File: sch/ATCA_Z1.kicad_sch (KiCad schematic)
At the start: 1 part, among them P10 1766500-1

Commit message: added magjacks
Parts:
- P10: footprint KIT_Connector:TE_1766500-1 -> project:TE_1766500-1
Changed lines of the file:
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@@
       (effects (font (size 1.27 1.27)))
     )
-    (property "Footprint" "KIT_Connector:TE_1766500-1" (at 144.78 92.71 0)
+    (property "Footprint" "project:TE_1766500-1" (at 144.78 92.71 0)
       (effects (font (size 1.27 1.27)) hide)
     )

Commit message: Project recovered
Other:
- title: ATCA Template -> ATCA Simple Loopback HUB
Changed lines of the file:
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@@
   (paper "A4")
   (title_block
-    (title "ATCA Template")
-    (date "2023-07-20")
+    (title "ATCA Simple Loopback HUB")
+    (date "2023-09-12")
     (rev "1.0")
     (company "Karlsruhe Institute of Technology (KIT)")
     (comment 1 "Institute for Data Processing and Electronics (IPE)")
     (comment 2 "Luis Ardila")
-    (comment 4 "Licensed under CERN-OHL-S-2.0")
+    (comment 3 "IPE-380-06")
+    (comment 4 "Licensed under CERN-OHL-P-2.0")
   )
   (no_connect (at 127 120.65))
@@
     (pin "9")
     (instances
-      (project "atca_simple_hub"
+      (project "atca-simple-loopback-hub"
         (path "/b1bf14e0-f6d2-45a7-b67f-6500a354b7ad/248439bf-2e2f-4e24-b510-c03a1ea34b90"
           (reference "P10") (unit 1)

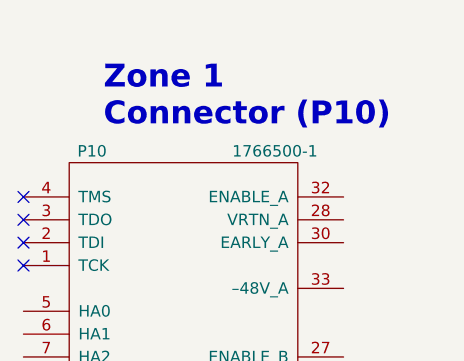
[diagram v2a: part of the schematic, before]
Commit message: organization of sub sheets
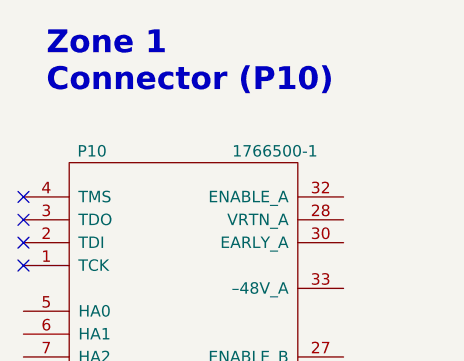
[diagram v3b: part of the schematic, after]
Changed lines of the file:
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@@
   (no_connect (at 127 107.95))
   (no_connect (at 127 110.49))
-  (text "Zone 1 \nConnector (P10)" (at 135.89 59.69 0)
+  (text "Zone 1 \nConnector (P10)" (at 129.54 55.88 0)
     (effects (font (size 2.54 2.54) (thickness 0.508) bold) (justify left bottom))
   )

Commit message: sch work
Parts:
- added C57, C58, C59, C60: 2.2uF, Capacitor_SMD:C_1206_3216Metric, symbol Device:C
- added C61, C62, C77, C78: 20nF, Capacitor_SMD:C_0805_2012Metric, symbol Device:C
- added C79, C80, C81: 100uF, Capacitor_THT:CP_Radial_D16.0mm_P7.50mm, symbol Device:C_Polarized
- added C82, C84: 22uF, Capacitor_SMD:C_0805_2012Metric, symbol Device:C
- added F1, F4: 1A, KIT_Fuse:SM2410, symbol Device:Fuse
- added F2, F3, F5, F6: 15A, KIT_Fuse:SM2410, symbol Device:Fuse
- added R35: DNP, KIT_Resistor_SMD:R_0805_2012Metric_DNP, symbol Device:R
- added R41, R42: 15, Resistor_SMD:R_2512_6332Metric, symbol Device:R
- added R7: 2k2, Resistor_SMD:R_0805_2012Metric_Pad1.20x1.40mm_HandSolder, symbol Device:R
- added R8: 4k7, Resistor_SMD:R_0402_1005Metric, symbol Device:R
- added U4: PIM400KZ, KIT_Converter_DCDC:PIM400KZ, symbol KIT_Converter_DCDC:PIM400KZ
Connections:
- net GNDPWR: now reaches P10.25 (SHELF_GND)
- net GNDPWR: now also U4.7 (SHELF_GND)
- net GND: now reaches P10.26 (LOGIC_GND)
- net GND: now also C61.2, C62.2, C77.2, C78.2, C82.2, C84.2, R35.2, U4.13 (LOGIC_GND)
- net Z1_EN_B: now reaches P10.27 (ENABLE_B)
- net Z1_EN_B: now also F4.2
- net Z1_VRTN_A: now reaches P10.28 (VRTN_A)
- net Z1_VRTN_A: now also F2.2
- net Z1_VRTN_B: now reaches P10.29 (VRTN_B)
- net Z1_VRTN_B: now also F5.2
- net Z1_EARLY_A: now reaches P10.30 (EARLY_A)
- net Z1_EARLY_A: now also R41.2
- net Z1_EARLY_B: now reaches P10.31 (EARLY_B)
- net Z1_EARLY_B: now also R42.2
- net Z1_EN_A: now reaches P10.32 (ENABLE_A)
- net Z1_EN_A: now also F1.2
- net Z1_-48V_A: now reaches P10.33 (–48V_A)
- net Z1_-48V_A: now also F3.2, R41.1
- net Z1_-48V_B: now reaches P10.34 (–48V_B)
- net Z1_-48V_B: now also F6.2, R42.1
- new net: R35.1, U4.10 (I2C_ADDR)
- new net: R7.2, U4.16 (TRIM_HLDP)
- new net +3V3: C84.1, R8.1, U4.9 (3V3)
- new net +5V: C82.1, U4.8 (5V0)
- new net BUS_N: C79.2, C80.2, C81.2, R7.1, U4.15 (-48V)
- new net BUS_P: U4.17 (VRET)
- new net PIM400_-48V_A: C57.2, C59.2, F3.1, U4.1 (-48V_A)
- new net PIM400_-48V_B: C58.2, C60.2, F6.1, U4.2 (-48V_B)
- new net PIM400_EN_A: F1.1, U4.5 (ENABLE_A)
- new net PIM400_EN_B: F4.1, U4.6 (ENABLE_B)
- new net PIM400_Shield_Plane: C61.1, C62.1, C77.1, C78.1
- new net PIM400_VRET_A: C57.1, C59.1, F2.1, U4.3 (VRET_A)
- new net PIM400_VRET_B: C58.1, C60.1, F5.1, U4.4 (VRET_B)
- new net SC_PIM.Alarm: R8.2, U4.14 (ALARM)
- new net SC_PIM.SCL: U4.12 (I2C_SCL)
- new net SC_PIM.SDA: U4.11 (I2C_SDA)
- new net V_HLDP: C79.1, C80.1, C81.1, U4.18 (V_HLDP)
- no-connect marks 12 -> 24
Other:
- note added: "-48V Power"
- note added: "3.3V @ 3.6A"
- note added: "5V @ 150mA"
- note added: "CHANGE HOLDUP CAPS"
- note added: "I2C Address = 8'b0101_111X, 8'h5E, 7'h2F"
- note added: "V_HLDP = 91 V => R_TRIM = 2.2 k 5ms @ 400W => C_HLDP >= 572 uF 5ms @ 350W => C_HLDP >= 501 uF"
- note added: "check shield specs"
- moved on the sheet: P10

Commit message: before sch review
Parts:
- F1, F2, F3, F4, F5, F6: footprint KIT_Fuse:SM2410 -> project:SM2410
- R35: value DNP -> 10k; footprint KIT_Resistor_SMD:R_0805_2012Metric_DNP -> Resistor_SMD:R_0805_2012Metric; DNP DNP -> (none); stock DNP -> (none); now not fitted
- U4: footprint KIT_Converter_DCDC:PIM400KZ -> project:PIM400KZ
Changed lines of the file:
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@@
       (effects (font (size 1.27 1.27)))
     )
-    (property "Footprint" "KIT_Fuse:SM2410" (at 97.79 85.852 90)
+    (property "Footprint" "project:SM2410" (at 97.79 85.852 90)
       (effects (font (size 1.27 1.27)) hide)
     )
@@
       (effects (font (size 1.27 1.27)))
     )
-    (property "Footprint" "KIT_Fuse:SM2410" (at 97.79 78.232 90)
+    (property "Footprint" "project:SM2410" (at 97.79 78.232 90)
       (effects (font (size 1.27 1.27)) hide)
     )
@@
       (effects (font (size 1.27 1.27)))
     )
-    (property "Footprint" "KIT_Fuse:SM2410" (at 97.79 68.072 90)
+    (property "Footprint" "project:SM2410" (at 97.79 68.072 90)
       (effects (font (size 1.27 1.27)) hide)
     )
@@
       (effects (font (size 1.27 1.27)))
     )
-    (property "Footprint" "KIT_Fuse:SM2410" (at 91.44 57.912 90)
+    (property "Footprint" "project:SM2410" (at 91.44 57.912 90)
       (effects (font (size 1.27 1.27)) hide)
     )
@@
   )
   (symbol (lib_id "Device:R") (at 210.82 92.71 90) (unit 1)
-    (in_bom no) (on_board yes) (dnp no)
+    (in_bom no) (on_board yes) (dnp yes) (fields_autoplaced)
     (property "Reference" "R35" (at 210.82 96.52 90)
       (effects (font (size 1.27 1.27)))
     )
-    (property "Value" "DNP" (at 210.82 99.06 90)
-      (effects (font (size 1.27 1.27)))
-    )
-    (property "Footprint" "KIT_Resistor_SMD:R_0805_2012Metric_DNP" (at 210.82 94.488 90)
+    (property "Value" "10k" (at 210.82 99.06 90)
+      (effects (font (size 1.27 1.27)))
+    )
+    (property "Footprint" "Resistor_SMD:R_0805_2012Metric" (at 210.82 94.488 90)
       (effects (font (size 1.27 1.27)) hide)
     )
@@
       (effects (font (size 1.27 1.27)) hide)
     )
-    (property "DNP" "DNP" (at 210.82 92.71 90)
-      (effects (font (size 1.27 1.27)))
-    )
-    (property "stock" "DNP" (at 210.82 92.71 0)
-      (effects (font (size 1.27 1.27)) hide)
-    )
     (pin "1")
     (pin "2")
@@
       (effects (font (size 1.27 1.27)))
     )
-    (property "Footprint" "KIT_Converter_DCDC:PIM400KZ" (at 166.37 74.93 0)
+    (property "Footprint" "project:PIM400KZ" (at 166.37 74.93 0)
       (effects (font (size 1.27 1.27)) hide)
     )
@@
       (effects (font (size 1.27 1.27)))
     )
-    (property "Footprint" "KIT_Fuse:SM2410" (at 97.79 60.452 90)
+    (property "Footprint" "project:SM2410" (at 97.79 60.452 90)
       (effects (font (size 1.27 1.27)) hide)
     )
@@
       (effects (font (size 1.27 1.27)))
     )
-    (property "Footprint" "KIT_Fuse:SM2410" (at 91.44 75.692 90)
-      (effects (font (size 1.27 1.27)) hide)
-    )
+    (property "Footprint" "project:SM2410" (at 91.44 75.692 90)
+      (effects (font (size 1.27 1.27)) hide)
+    )

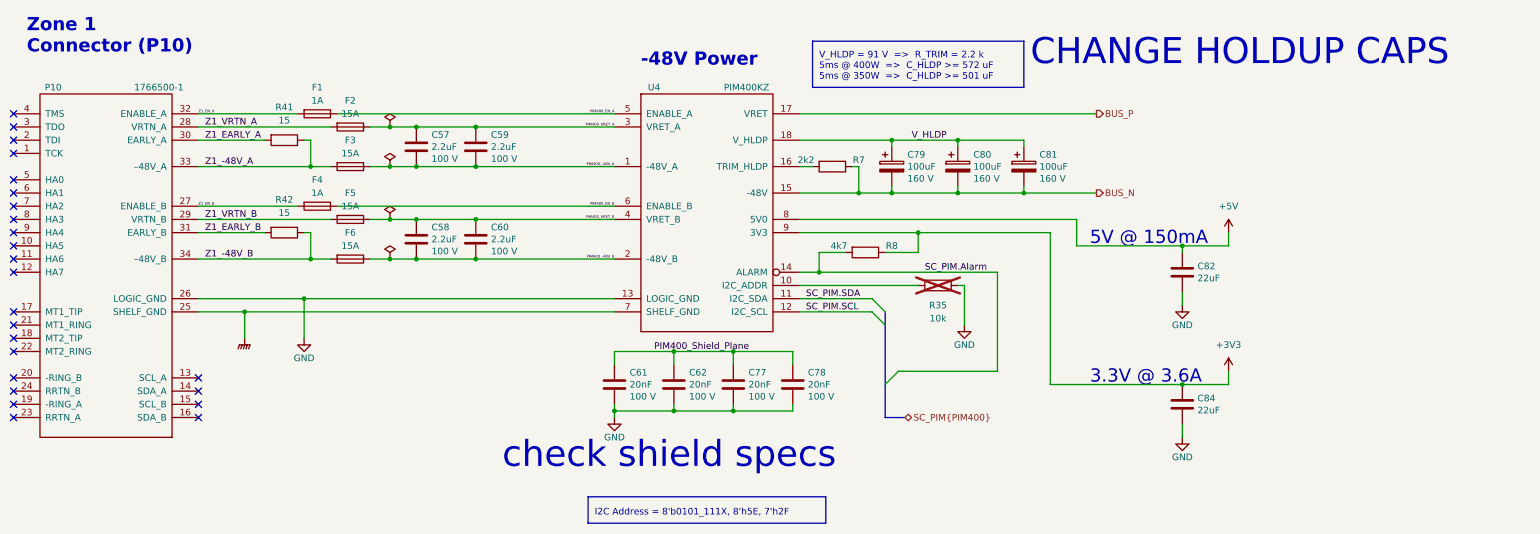
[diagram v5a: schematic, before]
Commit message: started changes from review
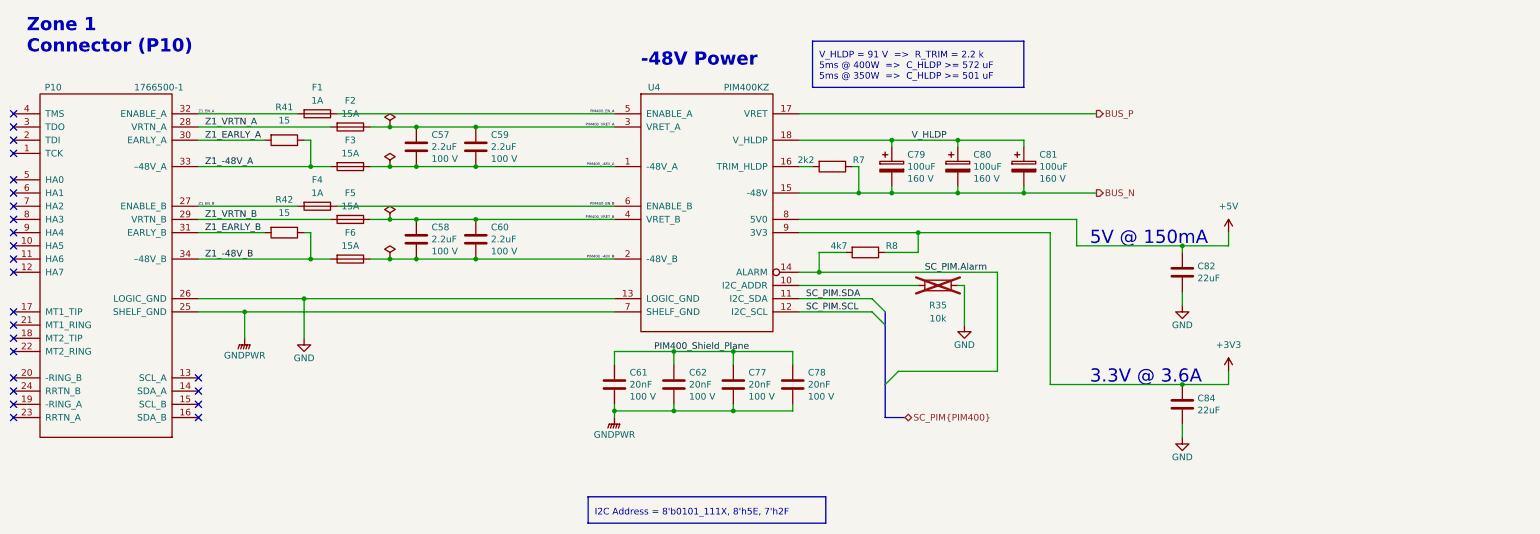
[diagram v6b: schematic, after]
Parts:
- C79, C80, C81: footprint Capacitor_THT:CP_Radial_D16.0mm_P7.50mm -> Capacitor_SMD:CP_Elec_18x22; digikey# (none) -> 493-UUJ2C101MNJ1MSCT-ND; manf# UCS2C101MHD6 -> UUJ2C101MNJ1MS; mouser# 647-UCS2C101MHD6 -> UUJ2C101MNJ1MS
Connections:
- net GND: no longer C61.2, C62.2, C77.2, C78.2
- net GNDPWR: now also C61.2, C62.2, C77.2, C78.2
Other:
- note removed: "CHANGE HOLDUP CAPS"
- note removed: "check shield specs"
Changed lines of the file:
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@@
     (effects (font (size 2.54 2.54)) (justify left bottom))
-  )
-  (text "CHANGE HOLDUP CAPS " (at 228.6 50.8 0)
-    (effects (font (size 5 5)) (justify left bottom))
   )
   (text "Zone 1 \nConnector (P10)" (at 35.56 48.26 0)
@@
     (at 187.96 53.34 0)
     (effects (font (size 1.27 1.27)) (justify left bottom))
-  )
-  (text "check shield specs\n" (at 127 128.27 0)
-    (effects (font (size 5 5)) (justify left bottom))
   )
   (text "I2C Address = 8'b0101_111X, 8'h5E, 7'h2F" (at 144.78 137.16 0)
@@
       (effects (font (size 1.27 1.27)) (justify left))
     )
-    (property "Footprint" "Capacitor_THT:CP_Radial_D16.0mm_P7.50mm" (at 202.8952 73.66 0)
+    (property "Footprint" "Capacitor_SMD:CP_Elec_18x22" (at 202.8952 73.66 0)
       (effects (font (size 1.27 1.27)) hide)
     )
@@
       (effects (font (size 1.27 1.27)) (justify left))
     )
+    (property "manf" "Nichicon" (at 201.93 69.85 0)
+      (effects (font (size 1.27 1.27)) hide)
+    )
+    (property "manf#" "UUJ2C101MNJ1MS" (at 201.93 69.85 0)
+      (effects (font (size 1.27 1.27)) hide)
+    )
     (property "rs#" "" (at 201.93 69.85 0)
       (effects (font (size 1.27 1.27)) hide)
     )
-    (property "digikey#" "" (at 201.93 69.85 0)
-      (effects (font (size 1.27 1.27)) hide)
-    )
-    (property "manf" "Nichicon" (at 201.93 69.85 0)
-      (effects (font (size 1.27 1.27)) hide)
-    )
-    (property "manf#" "UCS2C101MHD6" (at 201.93 69.85 0)
-      (effects (font (size 1.27 1.27)) hide)
-    )
-    (property "mouser#" "647-UCS2C101MHD6" (at 201.93 69.85 0)
+    (property "digikey#" "493-UUJ2C101MNJ1MSCT-ND" (at 201.93 69.85 0)
+      (effects (font (size 1.27 1.27)) hide)
+    )
+    (property "mouser#" "UUJ2C101MNJ1MS" (at 201.93 69.85 0)
       (effects (font (size 1.27 1.27)) hide)
     )
@@
       (effects (font (size 1.27 1.27)) (justify left))
     )
-    (property "Footprint" "Capacitor_THT:CP_Radial_D16.0mm_P7.50mm" (at 228.2952 73.66 0)
+    (property "Footprint" "Capacitor_SMD:CP_Elec_18x22" (at 228.2952 73.66 0)
       (effects (font (size 1.27 1.27)) hide)
     )
@@
       (effects (font (size 1.27 1.27)) hide)
     )
-    (property "digikey#" "" (at 227.33 69.85 0)
+    (property "digikey#" "493-UUJ2C101MNJ1MSCT-ND" (at 227.33 69.85 0)
       (effects (font (size 1.27 1.27)) hide)
     )
@@
       (effects (font (size 1.27 1.27)) hide)
     )
-    (property "manf#" "UCS2C101MHD6" (at 227.33 69.85 0)
-      (effects (font (size 1.27 1.27)) hide)
-    )
-    (property "mouser#" "647-UCS2C101MHD6" (at 227.33 69.85 0)
+    (property "manf#" "UUJ2C101MNJ1MS" (at 227.33 69.85 0)
+      (effects (font (size 1.27 1.27)) hide)
+    )
+    (property "mouser#" "UUJ2C101MNJ1MS" (at 227.33 69.85 0)
       (effects (font (size 1.27 1.27)) hide)
     )
@@
     )
   )
-  (symbol (lib_id "power:GND") (at 148.59 118.11 0) (unit 1)
-    (in_bom yes) (on_board yes) (dnp no)
-    (property "Reference" "#PWR0100" (at 148.59 124.46 0)
-      (effects (font (size 1.27 1.27)) hide)
-    )
-    (property "Value" "GND" (at 148.59 121.92 0)
-      (effects (font (size 1.27 1.27)))
-    )
-    (property "Footprint" "" (at 148.59 118.11 0)
-      (effects (font (size 1.27 1.27)) hide)
-    )
-    (property "Datasheet" "" (at 148.59 118.11 0)
-      (effects (font (size 1.27 1.27)) hide)
-    )
-    (pin "1")
-    (instances
-      (project "atca-simple-loopback-hub"
-        (path "/b1bf14e0-f6d2-45a7-b67f-6500a354b7ad/248439bf-2e2f-4e24-b510-c03a1ea34b90"
-          (reference "#PWR0100") (unit 1)
-        )
-      )
-    )
-  )
   (symbol (lib_id "Device:Fuse") (at 97.79 80.01 270) (unit 1)
     (in_bom yes) (on_board yes) (dnp no) (fields_autoplaced)
@@
         (path "/b1bf14e0-f6d2-45a7-b67f-6500a354b7ad/248439bf-2e2f-4e24-b510-c03a1ea34b90"
           (reference "F1") (unit 1)
+        )
+      )
+    )
+  )
+  (symbol (lib_id "power:GNDPWR") (at 148.59 118.11 0) (unit 1)
+    (in_bom yes) (on_board yes) (dnp no)
+    (property "Reference" "#PWR0102" (at 148.59 123.19 0)
+      (effects (font (size 1.27 1.27)) hide)
+    )
+    (property "Value" "GNDPWR" (at 148.59 121.412 0)
+      (effects (font (size 1.27 1.27)))
+    )
+    (property "Footprint" "" (at 148.59 119.38 0)
+      (effects (font (size 1.27 1.27)) hide)
+    )
+    (property "Datasheet" "" (at 148.59 119.38 0)
+      (effects (font (size 1.27 1.27)) hide)
+    )
+    (pin "1")
+    (instances
+      (project "atca-simple-loopback-hub"
+        (path "/b1bf14e0-f6d2-45a7-b67f-6500a354b7ad/248439bf-2e2f-4e24-b510-c03a1ea34b90"
+          (reference "#PWR0102") (unit 1)
         )
       )
@@
       (effects (font (size 1.27 1.27)) hide)
     )
-    (property "Value" "~" (at 77.5716 106.7816 0)
+    (property "Value" "GNDPWR" (at 77.47 106.172 0)
       (effects (font (size 1.27 1.27)))
     )
@@
       (effects (font (size 1.27 1.27)) (justify left))
     )
-    (property "Footprint" "Capacitor_THT:CP_Radial_D16.0mm_P7.50mm" (at 215.5952 73.66 0)
+    (property "Footprint" "Capacitor_SMD:CP_Elec_18x22" (at 215.5952 73.66 0)
       (effects (font (size 1.27 1.27)) hide)
     )
@@
       (effects (font (size 1.27 1.27)) hide)
     )
-    (property "digikey#" "" (at 214.63 69.85 0)
+    (property "digikey#" "493-UUJ2C101MNJ1MSCT-ND" (at 214.63 69.85 0)
       (effects (font (size 1.27 1.27)) hide)
     )
@@
       (effects (font (size 1.27 1.27)) hide)
     )
-    (property "manf#" "UCS2C101MHD6" (at 214.63 69.85 0)
-      (effects (font (size 1.27 1.27)) hide)
-    )
-    (property "mouser#" "647-UCS2C101MHD6" (at 214.63 69.85 0)
-      (effects (font (size 1.27 1.27)) hide)
-    )
+    (property "manf#" "UUJ2C101MNJ1MS" (at 214.63 69.85 0)
+      (effects (font (size 1.27 1.27)) hide)
+    )
+    (property "mouser#" "UUJ2C101MNJ1MS" (at 214.63 69.85 0)
+      (effects (font (size 1.27 1.27)) hide)
+    )
